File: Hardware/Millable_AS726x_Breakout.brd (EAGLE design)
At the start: 40.6 x 35.6 mm, 24 parts, among them J2 Serial Interface, U1 AS726X, U3 4MB Flash

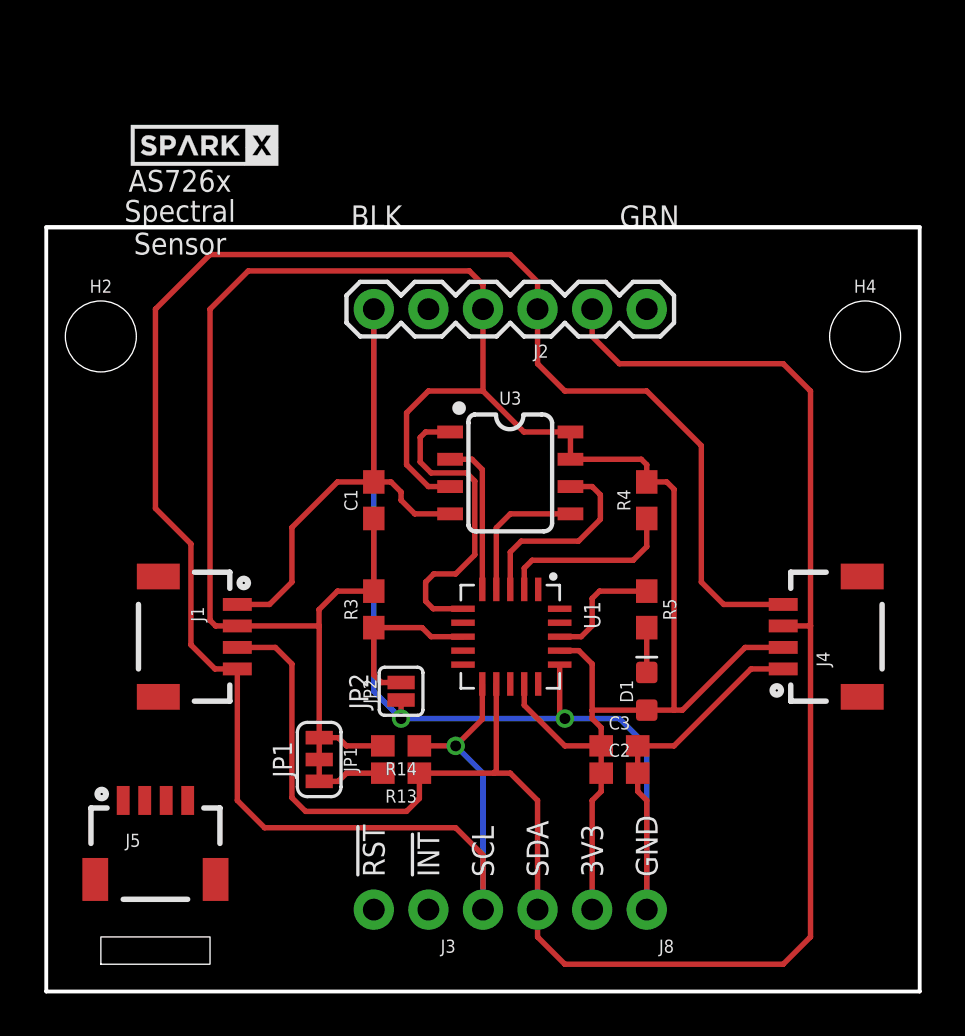
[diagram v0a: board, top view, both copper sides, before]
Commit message: Adding firmware, panel, and small fix to dimension on main layout.
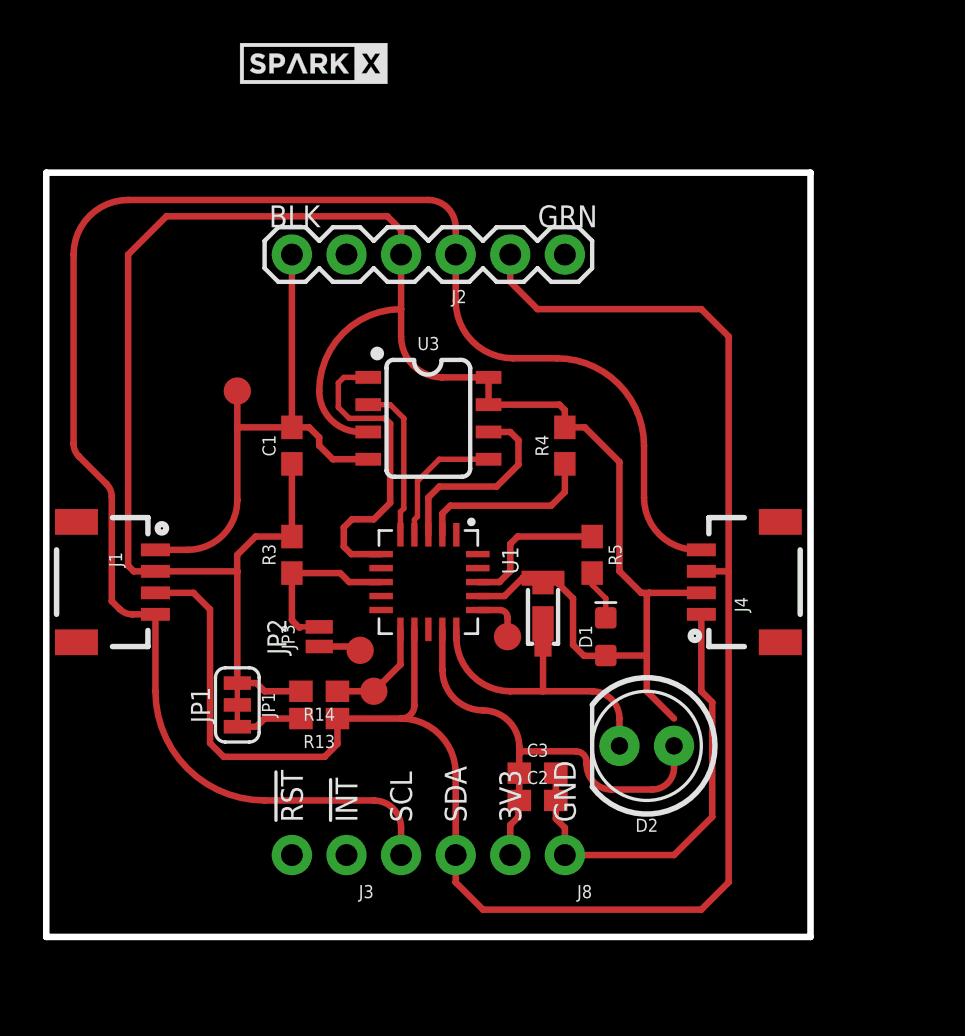
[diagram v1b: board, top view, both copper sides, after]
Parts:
- removed H2, H4: STAND-OFF, SparkFun-Hardware:STAND-OFF
- removed J5: (no value), SparkX:1X04_1MM_RA_STRESSRELIEF
- removed JP2: (no value), SparkFun-Jumpers:SMT-JUMPER_2_NO_SILK
- added D2: (no value), SparkFun-LED:LED_5MM
- added D3: LEDLD, SparkX:SUPER_BRIGHT_SMD_LED_1206
- added JP3: (no value), SparkX:SMT-JUMPER_2_NO_NO-SILK
- added TP1: (no value), SparkFun-Connectors:PAD.03X.05
- added TP2, TP3, TP4: TEST-POINT3X5, SparkFun-Connectors:PAD.03X.05
- moved LOGO4 21.3 mm to (19.1, 40.6)
- moved U$1 6.35 mm to (12.4, 40.6)
- moved J2 4.58 mm to (24.1, 31.8)
- moved J8 4.58 mm to (24.1, 3.81)
- moved R13 4.58 mm to (12.7, 10.2)
- moved R14 4.58 mm to (12.7, 11.4)
- moved R4 4.58 mm to (24.1, 22.9)
- moved J1 4.58 mm to (5.08, 16.5)
- moved J3 4.58 mm to (14.0, 3.81)
- moved R3 4.58 mm to (11.4, 17.8)
- moved C1 4.58 mm to (11.4, 22.9)
- moved J4 4.58 mm to (30.5, 16.5)
- moved U1 4.58 mm to (17.8, 16.5)
- moved JP1 4.58 mm to (8.89, 10.8)
- moved U3 4.58 mm to (17.8, 24.1)
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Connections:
- removed net N$1: JP2.2, R3.1, U1.8
- removed net VCC: J5.4
- new net I2C_ENB: JP3.2, R3.1, U1.8
- net 3.3V: now also D2.A, D3.A
- net GND: now also JP3.1, TP2.P$1, TP3.P$1, TP4.P$1; no longer J5.1, JP2.1
- net N$6: now also D2.K, D3.C
- net RX/SCL: now also TP1.P$1
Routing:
- net GND: track 81.3 -> 50.5 mm, vias 2 -> 0
- net RX/SCL: track 96.3 -> 83.4 mm, vias 1 -> 0
- net N$6: track 0.00 -> 12.7 mm
- net 3.3V: track 110.7 -> 121.2 mm
- net I2C_ENB: track 0.00 -> 7.96 mm
- net N$1: track 7.94 -> 0.00 mm
- net N$2: track 5.67 -> 6.94 mm
- net TX/SDA: track 86.2 -> 85.7 mm
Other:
- board size 40.6 x 35.6 mm -> 35.6 x 35.6 mm
- board text removed: "AS726x"
- board text removed: "Spectral Sensor"
